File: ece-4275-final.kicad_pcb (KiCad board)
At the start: 2 copper layers, 96.5 x 63.5 mm, 1 part, among them U1 ESP32-S3

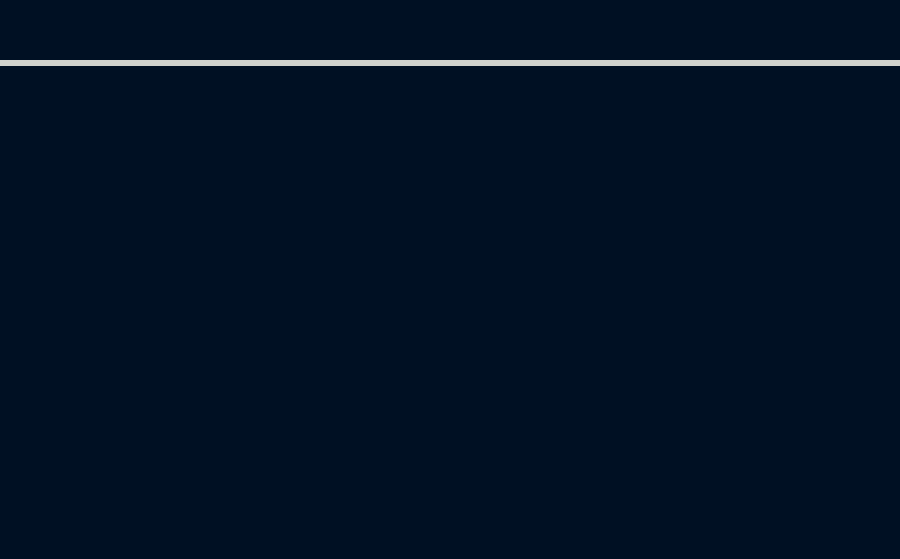
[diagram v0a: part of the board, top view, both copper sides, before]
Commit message: add library for local imports
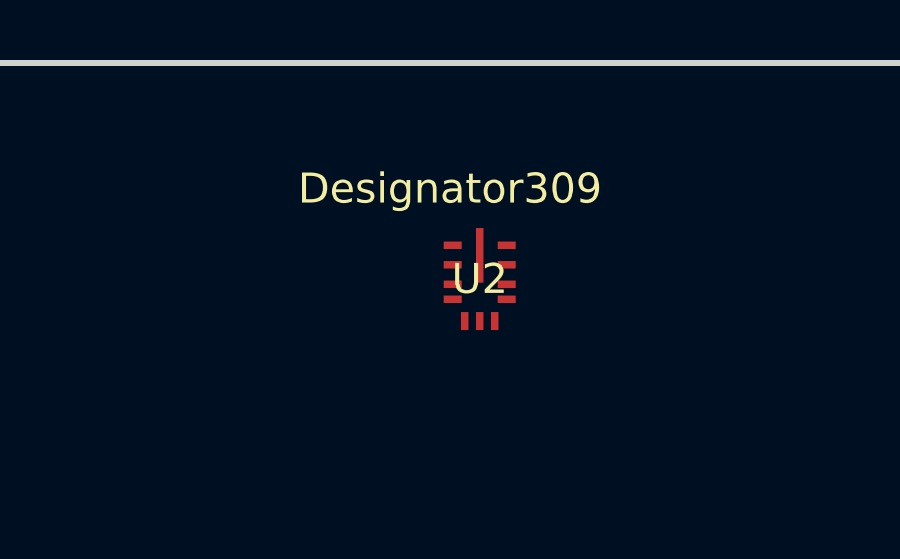
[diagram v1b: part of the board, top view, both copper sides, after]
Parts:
- added U2: LMR36015ARNXR, IMPORTS:LMR36015, F.Cu at (146.7, 55.2)

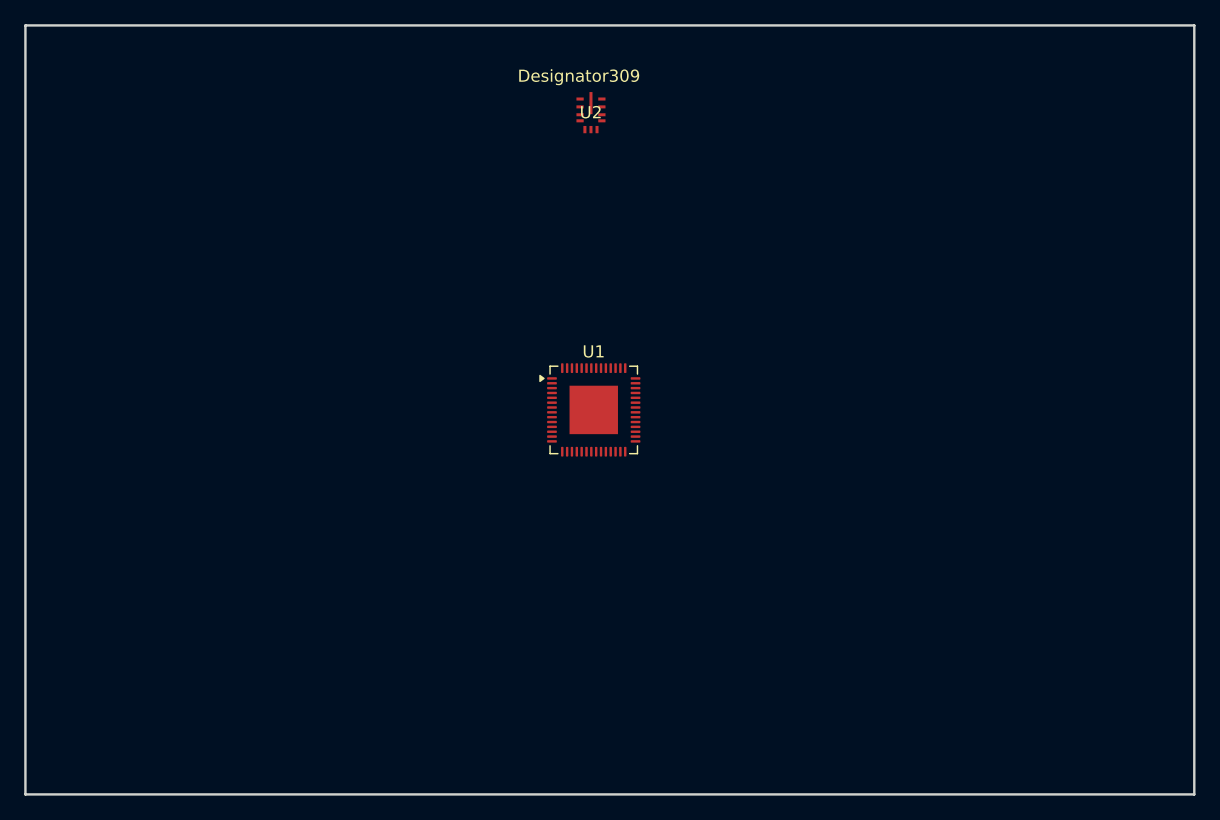
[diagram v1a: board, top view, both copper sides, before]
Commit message: add DCDC converter + LDO
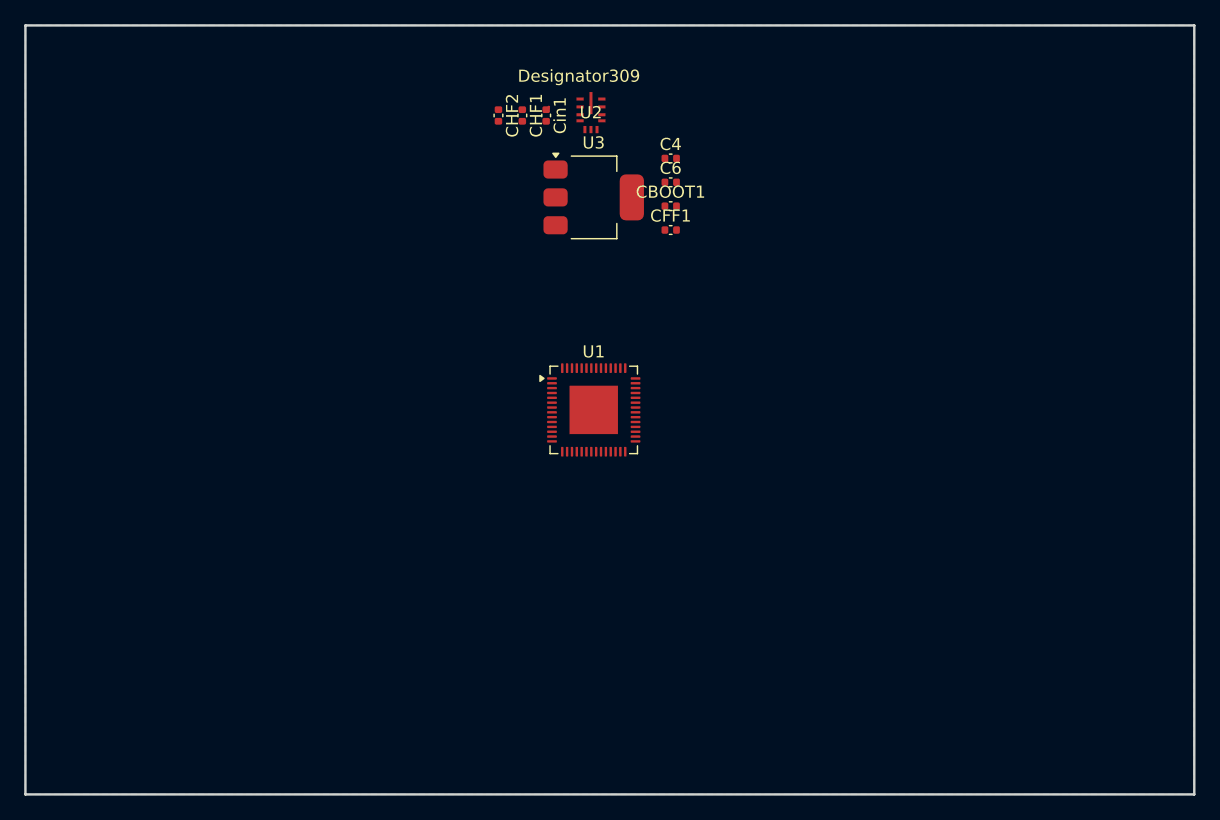
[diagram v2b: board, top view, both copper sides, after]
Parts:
- added C4: 1uF, Capacitor_SMD:C_0402_1005Metric, F.Cu at (153.3, 59.0)
- added C6: 4.7uF, Capacitor_SMD:C_0402_1005Metric, F.Cu at (153.3, 61.0)
- added CBOOT1: 0.1uF, Capacitor_SMD:C_0402_1005Metric, F.Cu at (153.3, 62.9)
- added CFF1: 20uF, Capacitor_SMD:C_0402_1005Metric, F.Cu at (153.3, 64.9)
- added CHF1: 220nF, Capacitor_SMD:C_0402_1005Metric, F.Cu at (141.0, 55.4)
- added CHF2: 220nF, Capacitor_SMD:C_0402_1005Metric, F.Cu at (139.1, 55.4)
- added Cin1: 4.7uF, Capacitor_SMD:C_0402_1005Metric, F.Cu at (143.0, 55.4)
- added U3: AMS1117-3.3, Package_TO_SOT_SMD:SOT-223-3_TabPin2, F.Cu at (146.9, 62.2)
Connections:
- U1 pad 20: unconnected-(U1-VDD3P3_RTC-Pad20) -> Net-(U1-VDD3P3_RTC)
- U1 pad 29: unconnected-(U1-VDD_SPI-Pad29) -> Net-(U1-VDD_SPI)
- U1 pad 46: unconnected-(U1-VDD3P3_CPU-Pad46) -> Net-(U1-VDD3P3_CPU)
- U1 pad 57: unconnected-(U1-GND-Pad57) -> GND
- U2 pad 1: unconnected-(U2-PGND-Pad1) -> GND
- U2 pad 11: unconnected-(U2-PGND-Pad11) -> GND
- U2 pad 12: unconnected-(U2-SW-Pad12) -> Net-(U2-SW)
- U2 pad 4: unconnected-(U2-BST-Pad4) -> Net-(U2-BST)
- U2 pad 5: unconnected-(U2-VCC-Pad5) -> Net-(U2-VCC)
- U2 pad 6: unconnected-(U2-AGND-Pad6) -> GND
- U2 pad 7: unconnected-(U2-FB-Pad7) -> Net-(U2-FB)
- U2 pad 8: unconnected-(U2-PG-Pad8) -> GND
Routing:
- added copper zone on B.Cu, net GND
